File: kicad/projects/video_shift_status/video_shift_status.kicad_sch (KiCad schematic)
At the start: 52 parts, among them J1 peripheral_addr_bus_connector, J2 peripheral_aux_connector, J3 peripheral_membank_connector, J4 Conn_01x16_Socket, J5 Conn_01x16_Socket, J6 video_aux, J7 Conn_01x03_Pin, J8 Conn_01x04_Socket, J9 Conn_02x06_Odd_Even, U1 74HC245, U10 74HC377, U11 74HC138, U12 74HC04, U13 74HC10, U14 74HC04, U15 74HC08, U2 74HC245, U3 74HC245, U4 74HC245, U5 74HC245, U6 74HC245, U7 74HC245, U8 74HC245, U9 74HC245

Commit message: Row and column order made consistent on top connectors. Bank Sel cursor tech checked.
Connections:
- net COL_IN_0: now also J5.1 (Pin_1), U1.11 (B8); no longer J5.9 (Pin_9), U5.11 (B8)
- net COL_IN_1: now also J5.2 (Pin_2), U1.12 (B7), U2.11 (B8); no longer J5.10 (Pin_10), U5.12 (B7), U6.11 (B8)
- net COL_IN_2: now also J5.3 (Pin_3), U1.13 (B6), U2.12 (B7), U3.11 (B8); no longer J5.11 (Pin_11), U5.13 (B6), U6.12 (B7), U7.11 (B8)
- net COL_IN_3: now also J5.4 (Pin_4), U1.14 (B5), U2.13 (B6), U3.12 (B7), U4.11 (B8); no longer J5.12 (Pin_12), U5.14 (B5), U6.13 (B6), U7.12 (B7), U8.11 (B8)
- net COL_IN_4: now also J5.5 (Pin_5), U1.15 (B4), U2.14 (B5), U3.13 (B6), U4.12 (B7); no longer J5.13 (Pin_13), U5.15 (B4), U6.14 (B5), U7.13 (B6), U8.12 (B7)
- net COL_IN_5: now also J5.6 (Pin_6), U1.16 (B3), U2.15 (B4), U3.14 (B5), U4.13 (B6); no longer J5.14 (Pin_14), U5.16 (B3), U6.15 (B4), U7.14 (B5), U8.13 (B6)
- net COL_IN_6: now also J5.7 (Pin_7), U1.17 (B2), U2.16 (B3), U3.15 (B4), U4.14 (B5); no longer J5.15 (Pin_15), U5.17 (B2), U6.16 (B3), U7.15 (B4), U8.14 (B5)
- net COL_IN_7: now also J5.8 (Pin_8), U1.18 (B1), U2.17 (B2), U3.16 (B3), U4.15 (B4); no longer J5.16 (Pin_16), U5.18 (B1), U6.17 (B2), U7.16 (B3), U8.15 (B4)
- net COL_OUT_0: now also J4.1 (Pin_1), U1.9 (A8), U2.9 (A8), U3.9 (A8), U4.9 (A8); no longer J4.9 (Pin_9), U5.9 (A8), U6.9 (A8), U7.9 (A8), U8.9 (A8)
- net COL_OUT_1: now also J4.2 (Pin_2), U1.8 (A7), U2.8 (A7), U3.8 (A7), U4.8 (A7); no longer J4.10 (Pin_10), U5.8 (A7), U6.8 (A7), U7.8 (A7), U8.8 (A7)
- net COL_OUT_2: now also J4.3 (Pin_3), U1.7 (A6), U2.7 (A6), U3.7 (A6), U4.7 (A6); no longer J4.11 (Pin_11), U5.7 (A6), U6.7 (A6), U7.7 (A6), U8.7 (A6)
- net COL_OUT_3: now also J4.4 (Pin_4), U1.6 (A5), U2.6 (A5), U3.6 (A5), U4.6 (A5); no longer J4.12 (Pin_12), U5.6 (A5), U6.6 (A5), U7.6 (A5), U8.6 (A5)
- net COL_OUT_4: now also J4.5 (Pin_5), U1.5 (A3), U2.5 (A3), U3.5 (A3), U4.5 (A3); no longer J4.13 (Pin_13), U5.5 (A3), U6.5 (A3), U7.5 (A3), U8.5 (A3)
- net COL_OUT_5: now also J4.6 (Pin_6), U1.4 (A3), U2.4 (A3), U3.4 (A3), U4.4 (A3); no longer J4.14 (Pin_14), U5.4 (A3), U6.4 (A3), U7.4 (A3), U8.4 (A3)
- net COL_OUT_6: now also J4.7 (Pin_7), U1.3 (A2), U2.3 (A2), U3.3 (A2), U4.3 (A2); no longer J4.15 (Pin_15), U5.3 (A2), U6.3 (A2), U7.3 (A2), U8.3 (A2)
- net COL_OUT_7: now also J4.8 (Pin_8), U1.2 (A1), U2.2 (A1), U3.2 (A1), U4.2 (A1); no longer J4.16 (Pin_16), U5.2 (A1), U6.2 (A1), U7.2 (A1), U8.2 (A1)
- net ROW_IN_0: now also J5.9 (Pin_9), U5.11 (B8); no longer J5.1 (Pin_1), U1.11 (B8)
- net ROW_IN_1: now also J5.10 (Pin_10), U5.12 (B7), U6.11 (B8); no longer J5.2 (Pin_2), U1.12 (B7), U2.11 (B8)
- net ROW_IN_2: now also J5.11 (Pin_11), U5.13 (B6), U6.12 (B7), U7.11 (B8); no longer J5.3 (Pin_3), U1.13 (B6), U2.12 (B7), U3.11 (B8)
- net ROW_IN_3: now also J5.12 (Pin_12), U5.14 (B5), U6.13 (B6), U7.12 (B7), U8.11 (B8); no longer J5.4 (Pin_4), U1.14 (B5), U2.13 (B6), U3.12 (B7), U4.11 (B8)
- net ROW_IN_4: now also J5.13 (Pin_13), U5.15 (B4), U6.14 (B5), U7.13 (B6), U8.12 (B7); no longer J5.5 (Pin_5), U1.15 (B4), U2.14 (B5), U3.13 (B6), U4.12 (B7)
- net ROW_IN_5: now also J5.14 (Pin_14), U5.16 (B3), U6.15 (B4), U7.14 (B5), U8.13 (B6); no longer J5.6 (Pin_6), U1.16 (B3), U2.15 (B4), U3.14 (B5), U4.13 (B6)
- net ROW_IN_6: now also J5.15 (Pin_15), U5.17 (B2), U6.16 (B3), U7.15 (B4), U8.14 (B5); no longer J5.7 (Pin_7), U1.17 (B2), U2.16 (B3), U3.15 (B4), U4.14 (B5)
- net ROW_IN_7: now also J5.16 (Pin_16), U5.18 (B1), U6.17 (B2), U7.16 (B3), U8.15 (B4); no longer J5.8 (Pin_8), U1.18 (B1), U2.17 (B2), U3.16 (B3), U4.15 (B4)
- net ROW_OUT_0: now also J4.9 (Pin_9), U5.9 (A8), U6.9 (A8), U7.9 (A8), U8.9 (A8); no longer J4.1 (Pin_1), U1.9 (A8), U2.9 (A8), U3.9 (A8), U4.9 (A8)
- net ROW_OUT_1: now also J4.10 (Pin_10), U5.8 (A7), U6.8 (A7), U7.8 (A7), U8.8 (A7); no longer J4.2 (Pin_2), U1.8 (A7), U2.8 (A7), U3.8 (A7), U4.8 (A7)
- net ROW_OUT_2: now also J4.11 (Pin_11), U5.7 (A6), U6.7 (A6), U7.7 (A6), U8.7 (A6); no longer J4.3 (Pin_3), U1.7 (A6), U2.7 (A6), U3.7 (A6), U4.7 (A6)
- net ROW_OUT_3: now also J4.12 (Pin_12), U5.6 (A5), U6.6 (A5), U7.6 (A5), U8.6 (A5); no longer J4.4 (Pin_4), U1.6 (A5), U2.6 (A5), U3.6 (A5), U4.6 (A5)
- net ROW_OUT_4: now also J4.13 (Pin_13), U5.5 (A3), U6.5 (A3), U7.5 (A3), U8.5 (A3); no longer J4.5 (Pin_5), U1.5 (A3), U2.5 (A3), U3.5 (A3), U4.5 (A3)
- net ROW_OUT_5: now also J4.14 (Pin_14), U5.4 (A3), U6.4 (A3), U7.4 (A3), U8.4 (A3); no longer J4.6 (Pin_6), U1.4 (A3), U2.4 (A3), U3.4 (A3), U4.4 (A3)
- net ROW_OUT_6: now also J4.15 (Pin_15), U5.3 (A2), U6.3 (A2), U7.3 (A2), U8.3 (A2); no longer J4.7 (Pin_7), U1.3 (A2), U2.3 (A2), U3.3 (A2), U4.3 (A2)
- net ROW_OUT_7: now also J4.16 (Pin_16), U5.2 (A1), U6.2 (A1), U7.2 (A1), U8.2 (A1); no longer J4.8 (Pin_8), U1.2 (A1), U2.2 (A1), U3.2 (A1), U4.2 (A1)
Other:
- moved on the sheet: U1, U2, U3, U4, U5, U6, U7, U8

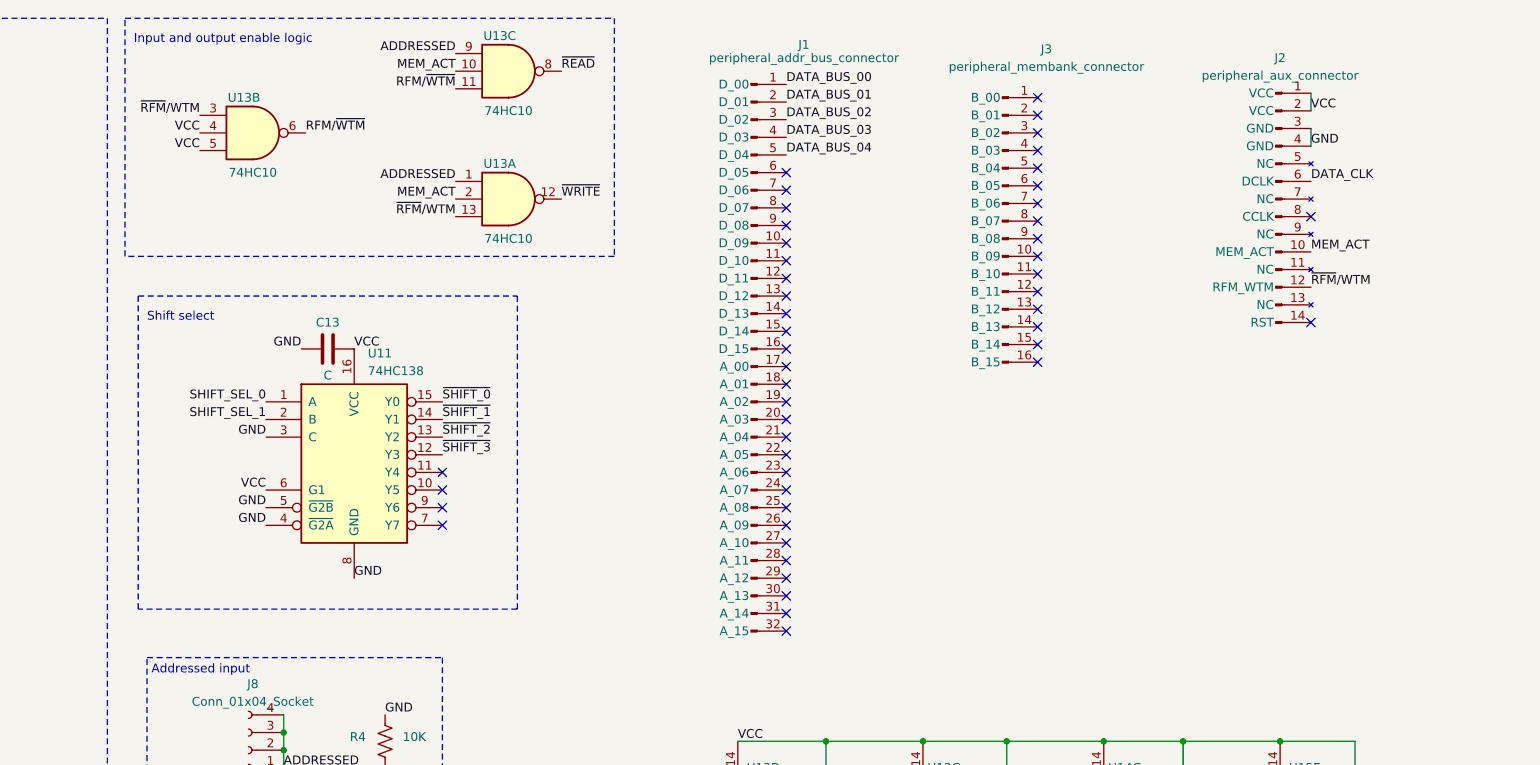
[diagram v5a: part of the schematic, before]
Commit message: Prep video out for RGB shuffle. Some work on shift status for tech checks, not complete yet.
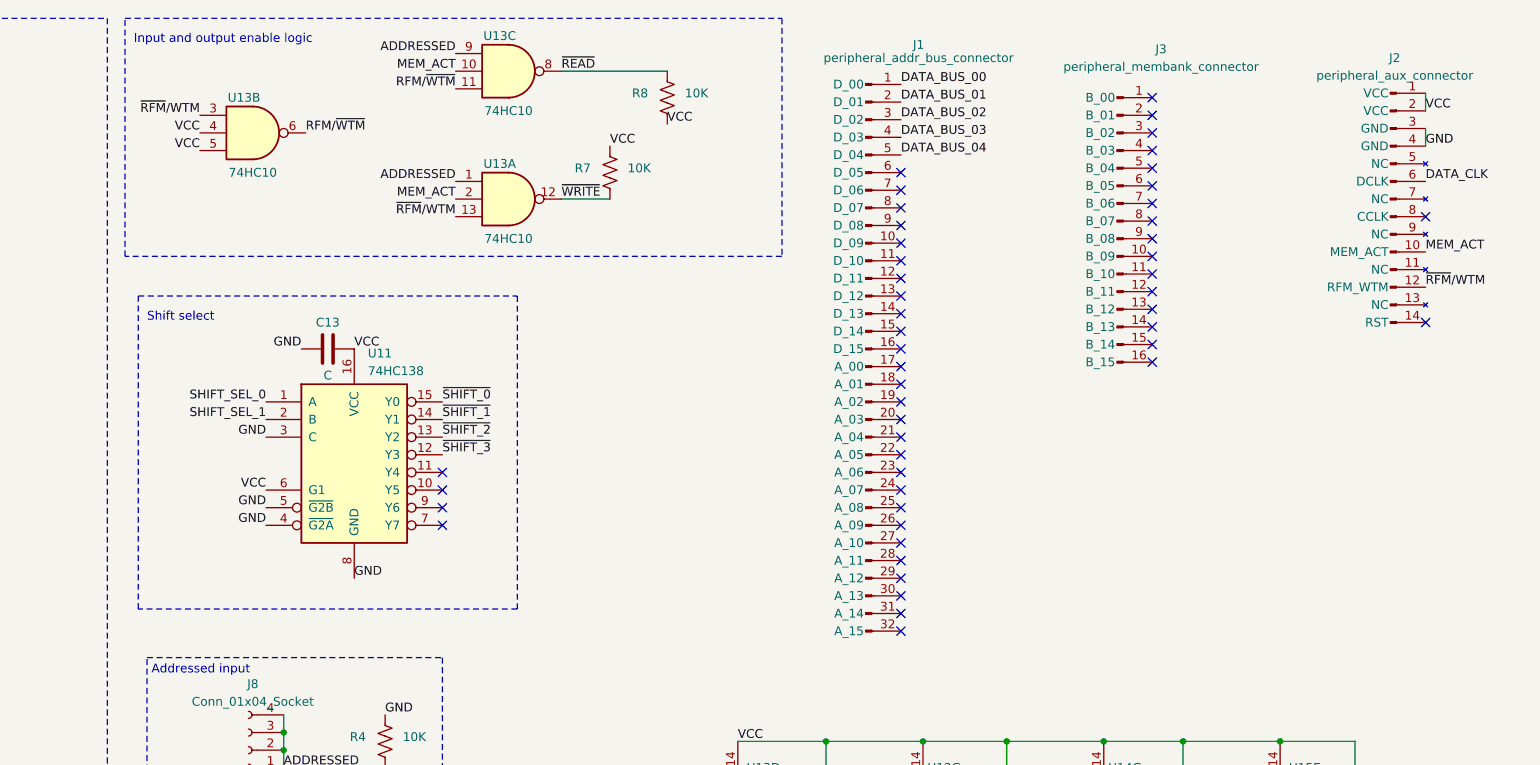
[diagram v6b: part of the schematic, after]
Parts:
- added R7, R8: 10K, Resistor_THT:R_Axial_DIN0207_L6.3mm_D2.5mm_P10.16mm_Horizontal, symbol Device:R_US
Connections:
- net VCC: now also R7.1, R8.2
- net ~{READ}: now also R8.1
- net ~{WRITE}: now also R7.2
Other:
- moved on the sheet: J1, J2, J3

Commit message: Video shift status and video output tech checked.
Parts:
- removed R2, R3: 10K, Resistor_THT:R_Axial_DIN0207_L6.3mm_D2.5mm_P10.16mm_Horizontal, symbol Device:R_US
- added J10: ENABLE DELAY, Connector_PinHeader_2.54mm:PinHeader_1x02_P2.54mm_Vertical, symbol Connector:Conn_01x02_Pin
- added RN2: 10K, Resistor_THT:R_Array_SIP5, symbol Device:R_Network04_US
- C97, C98, C99: value C_Polarized -> 33uF
- R1, R5, R6: value R_US -> 1K
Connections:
- net CHOSEN_PIX_CLK: now also J10.2 (Pin_2); no longer U12.5
- net GND: now also R7.2
- net VCC: now also RN2.1 (common); no longer R7.1
- net ~{SHIFT_0}: now also RN2.2 (R1)
- net ~{SHIFT_1}: now also RN2.3 (R2)
- net ~{SHIFT_2}: now also RN2.4 (R3)
- net ~{SHIFT_3}: now also RN2.5 (R4)
- net ~{WRITE}: no longer R7.2
- net at U9.16 (B3): now also RN1.5 (R4); no longer RN1.4 (R3)
- net at U9.17 (B2): now also RN1.6 (R5); no longer RN1.3 (R2)
- net at U9.18 (B1): now also RN1.7 (R6); no longer RN1.2 (R1)
- net at U9.2 (A1): now also RN1.2 (R1); no longer RN1.8 (R7)
- net at U9.3 (A2): now also RN1.3 (R2); no longer RN1.7 (R6)
- net at U9.4 (A3): now also RN1.4 (R3); no longer RN1.6 (R5)
- new net: J10.1 (Pin_1), R7.1, U12.5
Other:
- moved on the sheet: J7, RN1, U12A

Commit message: Finish updating rom counter to be 32 bit counter
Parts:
- C1, C10, C11, C12, C13, C14, C15, C2, C3, C4, C5, C6, C7, C8, C9: value C -> 0.1uF
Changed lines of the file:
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@@
   (paper "C")
   (bus_alias "ADDR_BUS" (members "ADDR_BUS_00" "ADDR_BUS_01" "ADDR_BUS_02" "ADDR_BUS_03" "ADDR_BUS_04" "ADDR_BUS_05" "ADDR_BUS_06" "ADDR_BUS_07" "ADDR_BUS_08" "ADDR_BUS_09" "ADDR_BUS_10" "ADDR_BUS_11" "ADDR_BUS_12" "ADDR_BUS_13" "ADDR_BUS_14" "ADDR_BUS_15"))
+  (bus_alias "DATA_BUS" (members "DATA_BUS_00" "DATA_BUS_01" "DATA_BUS_02" "DATA_BUS_03" "DATA_BUS_04" "DATA_BUS_05" "DATA_BUS_06" "DATA_BUS_07" "DATA_BUS_08" "DATA_BUS_09" "DATA_BUS_10" "DATA_BUS_11" "DATA_BUS_12" "DATA_BUS_13" "DATA_BUS_14" "DATA_BUS_15"))
+  (bus_alias "BANK_BUS" (members "BANK_BUS_00" "BANK_BUS_01" "BANK_BUS_02" "BANK_BUS_03" "BANK_BUS_04" "BANK_BUS_05" "BANK_BUS_06" "BANK_BUS_07" "BANK_BUS_08" "BANK_BUS_09" "BANK_BUS_10" "BANK_BUS_11" "BANK_BUS_12" "BANK_BUS_13" "BANK_BUS_14" "BANK_BUS_15"))
   (bus_alias "ROW_OUT_BUS" (members "ROW_OUT_00" "ROW_OUT_01" "ROW_OUT_02" "ROW_OUT_03" "ROW_OUT_04" "ROW_OUT_05" "ROW_OUT_06" "ROW_OUT_07"))
+  (bus_alias "COL_IN_BUS" (members "COL_IN_00" "COL_IN_01" "COL_IN_02" "COL_IN_03" "COL_IN_04" "COL_IN_05" "COL_IN_06" "COL_IN_07"))
   (bus_alias "" (members ))
   (bus_alias "ROW_IN_BUS" (members "ROW_IN_00" "ROW_IN_01" "ROW_IN_02" "ROW_IN_03" "ROW_IN_04" "ROW_IN_05" "ROW_IN_06" "ROW_IN_07"))
-  (bus_alias "BANK_BUS" (members "BANK_BUS_00" "BANK_BUS_01" "BANK_BUS_02" "BANK_BUS_03" "BANK_BUS_04" "BANK_BUS_05" "BANK_BUS_06" "BANK_BUS_07" "BANK_BUS_08" "BANK_BUS_09" "BANK_BUS_10" "BANK_BUS_11" "BANK_BUS_12" "BANK_BUS_13" "BANK_BUS_14" "BANK_BUS_15"))
-  (bus_alias "COL_IN_BUS" (members "COL_IN_00" "COL_IN_01" "COL_IN_02" "COL_IN_03" "COL_IN_04" "COL_IN_05" "COL_IN_06" "COL_IN_07"))
-  (bus_alias "DATA_BUS" (members "DATA_BUS_00" "DATA_BUS_01" "DATA_BUS_02" "DATA_BUS_03" "DATA_BUS_04" "DATA_BUS_05" "DATA_BUS_06" "DATA_BUS_07" "DATA_BUS_08" "DATA_BUS_09" "DATA_BUS_10" "DATA_BUS_11" "DATA_BUS_12" "DATA_BUS_13" "DATA_BUS_14" "DATA_BUS_15"))
   (junction (at 461.645 122.555) (diameter 0) (color 0 0 0 0)
   )
@@
       (effects (font (size 1.27 1.27)) (justify left))
     )
-    (property "Value" "C" (at 527.05 137.16 0)
+    (property "Value" "0.1uF" (at 527.05 137.16 0)
       (effects (font (size 1.27 1.27)) (justify left))
     )
@@
       (effects (font (size 1.27 1.27)))
     )
-    (property "Value" "C" (at 57.785 136.525 90)
+    (property "Value" "0.1uF" (at 57.785 136.525 90)
       (effects (font (size 1.27 1.27)))
     )
@@
       (effects (font (size 1.27 1.27)))
     )
-    (property "Value" "C" (at 156.21 136.525 90)
+    (property "Value" "0.1uF" (at 156.21 136.525 90)
       (effects (font (size 1.27 1.27)))
     )
@@
       (effects (font (size 1.27 1.27)))
     )
-    (property "Value" "C" (at 57.785 29.21 90)
+    (property "Value" "0.1uF" (at 57.785 29.21 90)
       (effects (font (size 1.27 1.27)))
     )
@@
       (effects (font (size 1.27 1.27)))
     )
-    (property "Value" "C" (at 156.21 190.5 90)
+    (property "Value" "0.1uF" (at 156.21 190.5 90)
       (effects (font (size 1.27 1.27)))
     )
@@
       (effects (font (size 1.27 1.27)))
     )
-    (property "Value" "C" (at 57.785 83.185 90)
+    (property "Value" "0.1uF" (at 57.785 83.185 90)
       (effects (font (size 1.27 1.27)))
     )
@@
       (effects (font (size 1.27 1.27)))
     )
-    (property "Value" "C" (at 375.92 69.85 90)
+    (property "Value" "0.1uF" (at 375.92 69.85 90)
       (effects (font (size 1.27 1.27)))
     )
@@
       (effects (font (size 1.27 1.27)) (justify left))
     )
-    (property "Value" "C" (at 450.85 137.16 0)
+    (property "Value" "0.1uF" (at 450.85 137.16 0)
       (effects (font (size 1.27 1.27)) (justify left))
     )
@@
       (effects (font (size 1.27 1.27)))
     )
-    (property "Value" "C" (at 248.92 100.965 0)
+    (property "Value" "0.1uF" (at 248.92 100.965 0)
       (effects (font (size 1.27 1.27)))
     )
@@
       (effects (font (size 1.27 1.27)))
     )
-    (property "Value" "C" (at 156.21 83.185 90)
+    (property "Value" "0.1uF" (at 156.21 83.185 90)
       (effects (font (size 1.27 1.27)))
     )
@@
       (effects (font (size 1.27 1.27)))
     )
-    (property "Value" "C" (at 57.785 190.5 90)
+    (property "Value" "0.1uF" (at 57.785 190.5 90)
       (effects (font (size 1.27 1.27)))
     )
@@
       (effects (font (size 1.27 1.27)) (justify left))
     )
-    (property "Value" "C" (at 502.285 137.16 0)
+    (property "Value" "0.1uF" (at 502.285 137.16 0)
       (effects (font (size 1.27 1.27)) (justify left))
     )
@@
       (effects (font (size 1.27 1.27)) (justify left))
     )
-    (property "Value" "C" (at 476.885 137.16 0)
+    (property "Value" "0.1uF" (at 476.885 137.16 0)
       (effects (font (size 1.27 1.27)) (justify left))
     )
@@
       (effects (font (size 1.27 1.27)))
     )
-    (property "Value" "C" (at 156.21 29.21 90)
+    (property "Value" "0.1uF" (at 156.21 29.21 90)
       (effects (font (size 1.27 1.27)))
     )
@@
       (effects (font (size 1.27 1.27)))
     )
-    (property "Value" "C" (at 271.78 50.8 0)
+    (property "Value" "0.1uF" (at 271.78 50.8 0)
       (effects (font (size 1.27 1.27)))
     )
